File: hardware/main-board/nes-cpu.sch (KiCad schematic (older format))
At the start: 36 parts, among them SW1 NES Reset, U10 74HCT00, U11 PCA9564, U3 74LVC1404, U4 RP2A03, U5 74HCT138, U6 LM4889, U7 AS6C6264, U8 MCP40D17, U9 AT28C64B, Y1 21.5 MHz

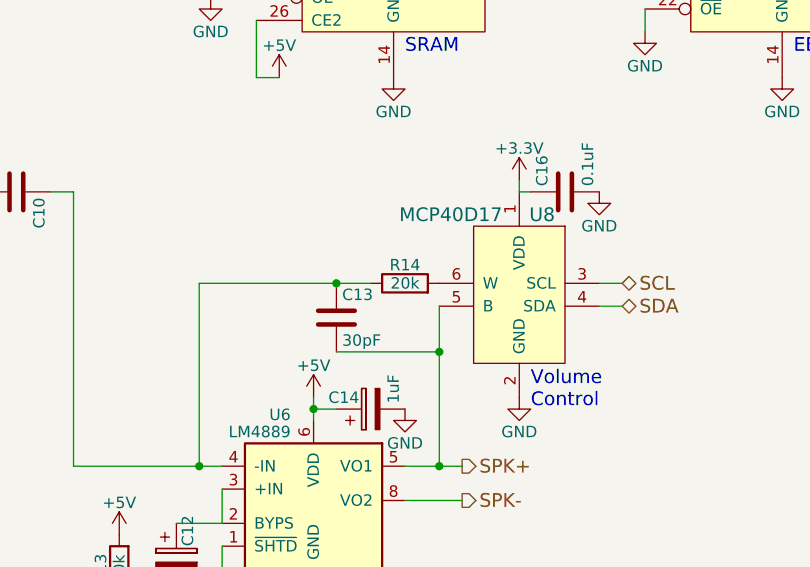
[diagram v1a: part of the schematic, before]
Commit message: Change amplifier gain resistor from 20k to 4.7k
In testing, the minimum volume with 10k was still a little bit too loud,
so going with 4.7k for now. This is easily adjustible in the future
without any actual board layout changes.

Fixes #4
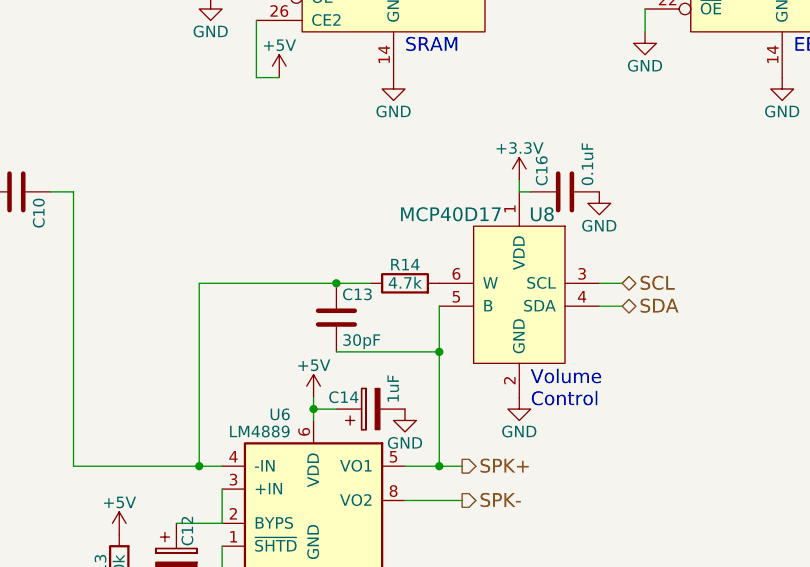
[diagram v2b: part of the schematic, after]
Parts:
- R14: value 20k -> 4.7k; Description RES SMD 20K OHM 5% 1/8W 0805 -> RES SMD 4.7K OHM 5% 1/8W 0805; Manufacturer PN CRCW080520K0JNEA -> CRCW08054K70JNEA; Supplier PN 541-20KACT-ND -> 541-4.7KACT-ND
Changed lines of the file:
@@
 P 6300 3950
 F 0 "R14" V 6380 3950 50  0000 C CNN
-F 1 "20k" V 6300 3950 50  0000 C CNN
+F 1 "4.7k" V 6300 3950 50  0000 C CNN
 F 2 "Resistor_SMD:R_0805_2012Metric" V 6230 3950 50  0001 C CNN
 F 3 "http://www.vishay.com/docs/20035/dcrcwe3.pdf" H 6300 3950 50  0001 C CNN
-F 4 "RES SMD 20K OHM 5% 1/8W 0805" H 6300 3950 60  0001 C CNN "Description"
+F 4 "RES SMD 4.7K OHM 5% 1/8W 0805" H 6300 3950 60  0001 C CNN "Description"
 F 5 "Vishay Dale" H 6300 3950 60  0001 C CNN "Manufacturer"
-F 6 "CRCW080520K0JNEA" H 6300 3950 60  0001 C CNN "Manufacturer PN"
+F 6 "CRCW08054K70JNEA" H 6300 3950 60  0001 C CNN "Manufacturer PN"
 F 7 "Digi-Key" H 6380 4050 50  0001 C CNN "Supplier"
-F 8 "541-20KACT-ND" H 6300 3950 60  0001 C CNN "Supplier PN"
+F 8 "541-4.7KACT-ND" H 6300 3950 60  0001 C CNN "Supplier PN"
 	1    6300 3950
 	0    -1   -1   0

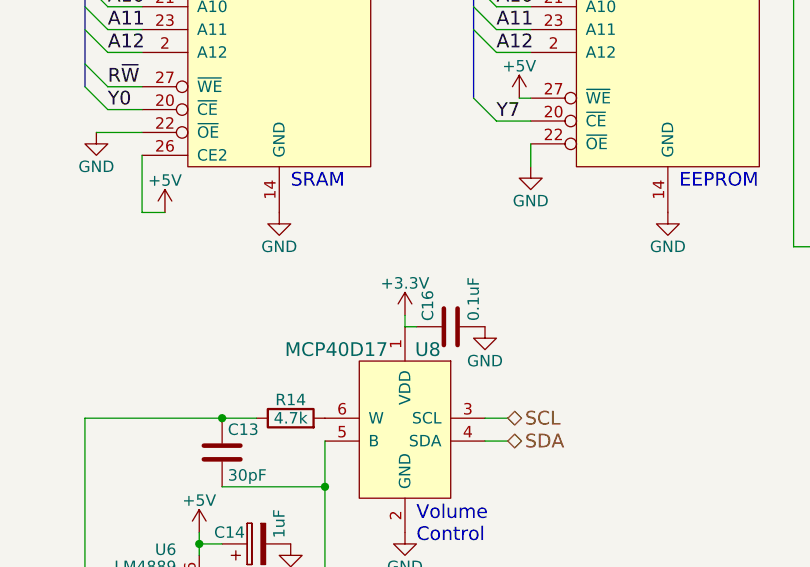
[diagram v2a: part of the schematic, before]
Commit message: Changed U8 Vdd from 3.3V to 5V
Had to reroute a few other traces in the process of doing this, and was
able to remove some vias from a 3.3V line. Also added some stitching
vias to re-connect the ground plane that changed as a result.
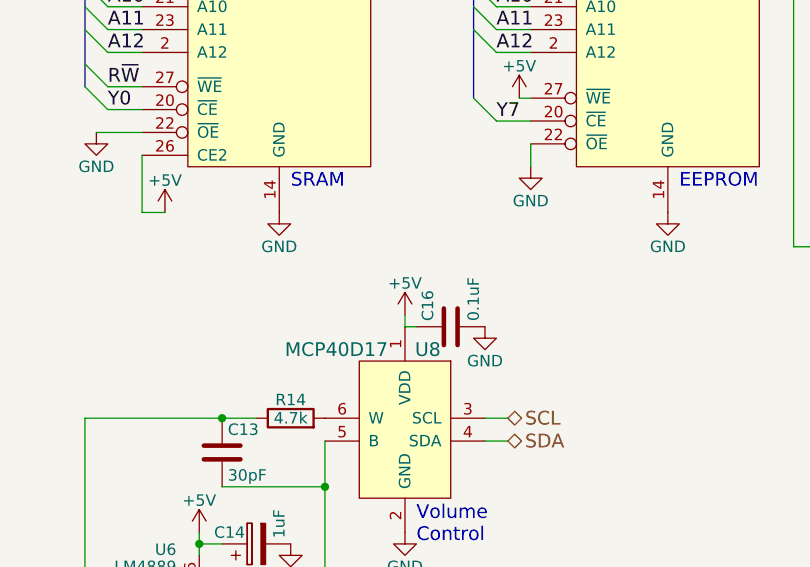
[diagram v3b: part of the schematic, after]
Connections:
- net +3V3: no longer C16.1, U8.1 (VDD)
- net +5V: now also C16.1, U8.1 (VDD)
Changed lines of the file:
@@
-$EndComp
-$Comp
-L +3.3V #PWR051
-U 1 1 5A64F776
-P 6800 3500
-F 0 "#PWR051" H 6800 3350 50  0001 C CNN
-F 1 "+3.3V" H 6800 3640 50  0000 C CNN
-F 2 "" H 6800 3500 50  0001 C CNN
-F 3 "" H 6800 3500 50  0001 C CNN
-	1    6800 3500
-	1    0    0    -1
 $EndComp
 $Comp
@@
 Text Notes 600  1850 0    60   ~ 0
 Reset Button
+$Comp
+L +5V #PWR?
+U 1 1 5B2AA23C
+P 6800 3500
+F 0 "#PWR?" H 6800 3350 50  0001 C CNN
+F 1 "+5V" H 6800 3640 50  0000 C CNN
+F 2 "" H 6800 3500 50  0001 C CNN
+F 3 "" H 6800 3500 50  0001 C CNN
+	1    6800 3500
+	1    0    0    -1
+$EndComp
 $EndSCHEMATC

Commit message: Change U7 footprint to one that more closely matches the component
This involved adding a custom SOIC-28 footprint variant for the
AS6C6264.

This IC uses what it calls a "28-pin 330 mil SOP" package, which is not
in the standard libraries. Its closest match is KiCad's SOIC-28W, but it
is slightly wider and taller. This footprint and 3D model is based on
using the IC's datasheet and the reference datasheets from KiCad's
footprint and 3D model to determine small adjustments.

The replacement footprint is slightly wider, so some routing was
adjusted. However, it is mostly a drop-in replacement.

Fixes #1
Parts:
- U7: footprint Package_SO:SOIC-28W_7.5x17.9mm_P1.27mm -> lib_fp:SOIC-28W_8.636x18.491mm_P1.27mm
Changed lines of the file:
@@
 F 0 "U7" H 6250 2150 60  0000 C CNN
 F 1 "AS6C6264" H 6250 1950 60  0000 C CNN
-F 2 "Package_SO:SOIC-28W_7.5x17.9mm_P1.27mm" H 6250 1950 60  0001 C CNN
+F 2 "lib_fp:SOIC-28W_8.636x18.491mm_P1.27mm" H 6250 1950 60  0001 C CNN
 F 3 "https://www.alliancememory.com/wp-content/uploads/pdf/Alliance%20Memory_64K_AS6C6264v2.0July2017.pdf" H 6250 1950 60  0001 C CNN
 F 4 "IC SRAM 64KBIT 55NS 28SOP" H 6250 1950 60  0001 C CNN "Description"

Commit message: Swap U11 from SOIC to TSSOP footprint
This was a trivial part change, with quite extensive trace routing
changes.

Fixes #2
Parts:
- U11: footprint Package_SO:SOIC-20W_7.5x12.8mm_P1.27mm -> Package_SO:TSSOP-20_4.4x6.5mm_P0.65mm
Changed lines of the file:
@@
 F 0 "U11" H 9600 1850 60  0000 C CNN
 F 1 "PCA9564" H 9600 1750 60  0000 C CNN
-F 2 "Package_SO:SOIC-20W_7.5x12.8mm_P1.27mm" H 9550 1900 60  0001 C CNN
+F 2 "Package_SO:TSSOP-20_4.4x6.5mm_P0.65mm" H 9550 1900 60  0001 C CNN
 F 3 "https://www.nxp.com/docs/en/data-sheet/PCA9564.pdf" H 9550 1900 60  0001 C CNN
 F 4 "IC CTRL PARALLEL/I2C BUS 20-SOIC" H 9600 1650 60  0001 C CNN "Description"
-F 5 "PCA9564D,112" H 9600 1650 60  0001 C CNN "Manufacturer PN"
-F 6 "NXP" H 9600 1650 60  0001 C CNN "Manufacturer"
-F 7 "568-1062-5-ND" H 9600 1650 60  0001 C CNN "Supplier PN"
-F 8 "Digi-Key" H 9600 1650 60  0001 C CNN "Supplier"
+F 5 "NXP" H 9600 1650 60  0001 C CNN "Manufacturer"
+F 6 "PCA9564D,112" H 9600 1650 60  0001 C CNN "Manufacturer PN"
+F 7 "Digi-Key" H 9600 1650 60  0001 C CNN "Supplier"
+F 8 "568-1062-5-ND" H 9600 1650 60  0001 C CNN "Supplier PN"
 	1    9600 1650
 	1    0    0    -1

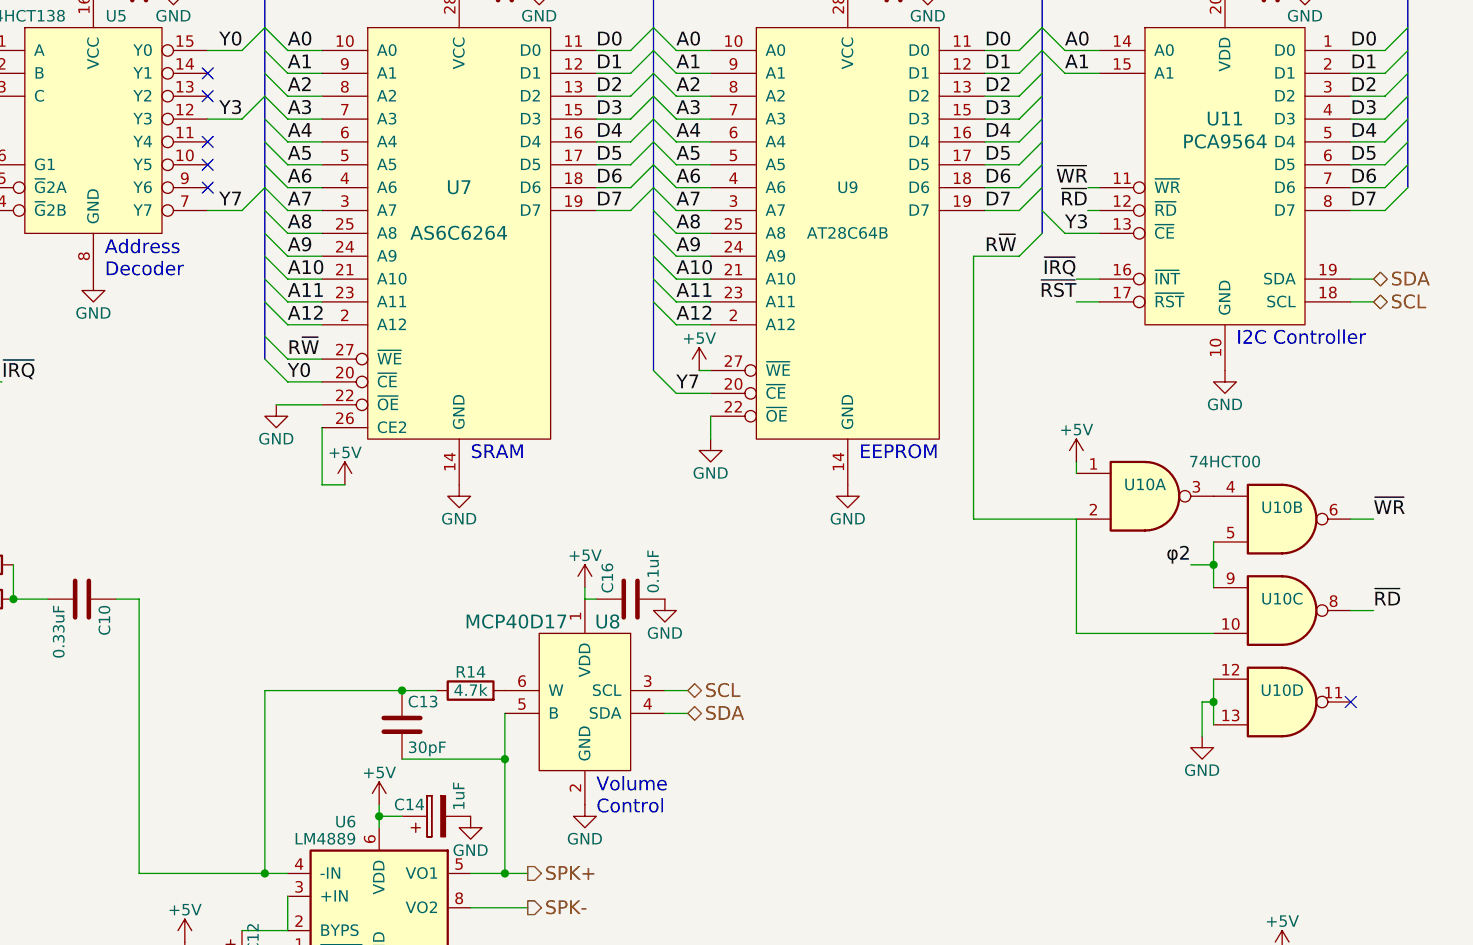
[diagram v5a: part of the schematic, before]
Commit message: Change SRAM address decoding to mirror it onto address $C000
To support the NES APU's DMC feature, we need sample memory placed
around address $C000. Since we're only using a tiny portion of our RAM,
the easiest way is to mirror the RAM onto both $0000 and $C000.

This can be accomplished with a spare NAND gate already in our circuit,
and the secondary non-inverting chip enable line of the SRAM chip. The
idea is that if either Y0 or Y6 is low, then the output of the NAND gate
will be high, and thus select the chip.

Fixes #7
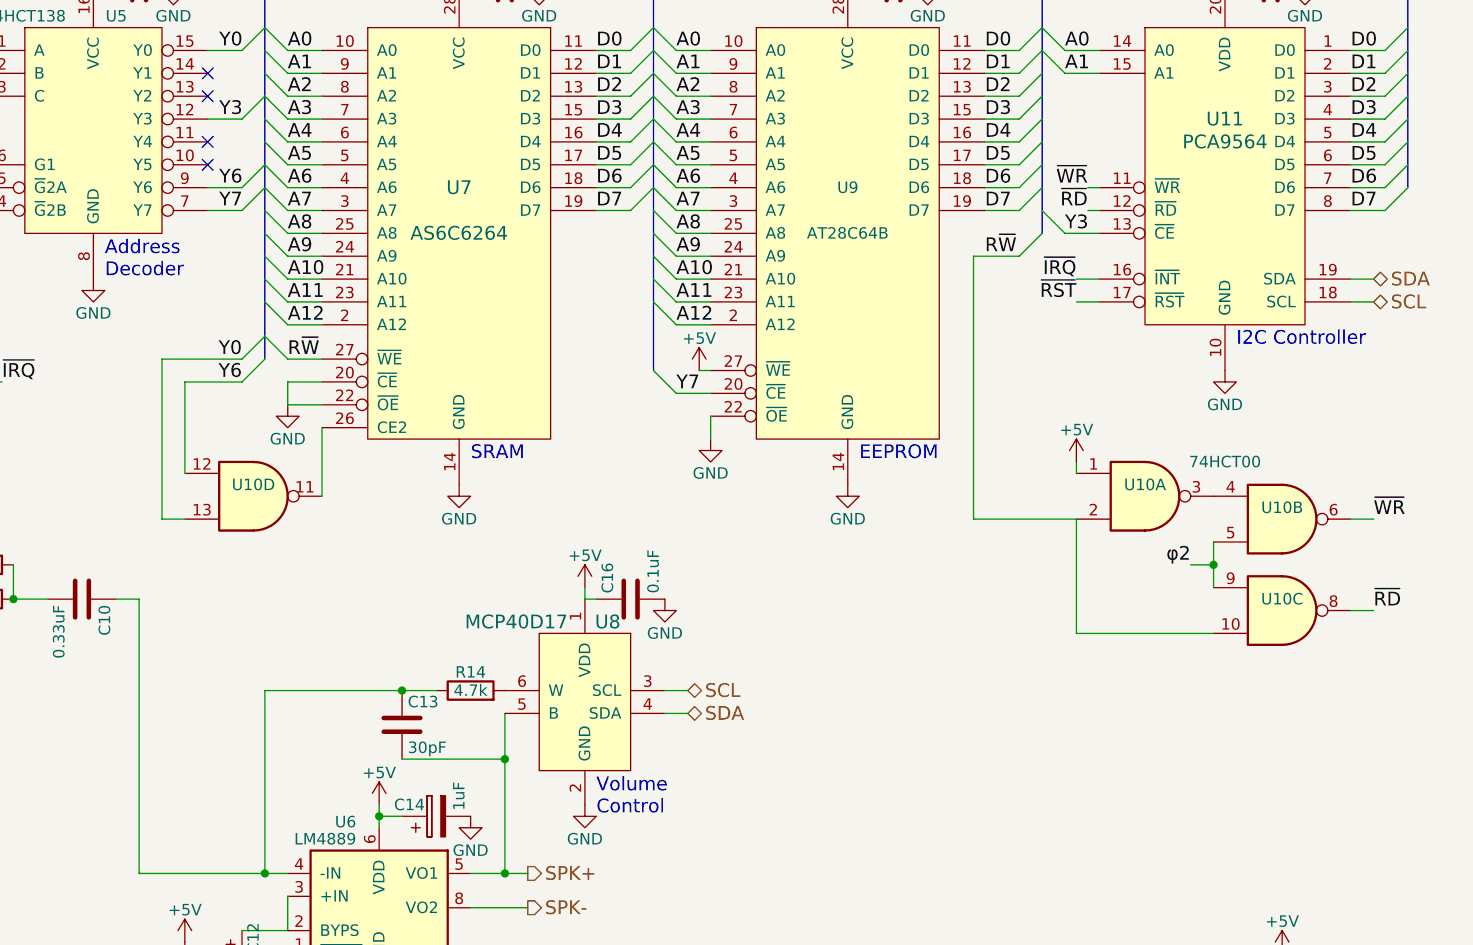
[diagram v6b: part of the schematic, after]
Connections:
- net +5V: no longer U7.26 (CE2)
- net GND: now also U7.20 (~CE); no longer U10.12, U10.13
- net Y0: now also U10.13; no longer U7.20 (~CE)
- net Y6: now reaches U5.9 (Y6)
- net Y6: now also U10.12
- net at U10.11: now also U7.26 (CE2)
- no-connect marks 10 -> 8
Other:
- moved on the sheet: U10D
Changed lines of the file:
@@
-$EndComp
-$Comp
-L +5V #PWR030
-U 1 1 5A482A40
-P 5750 3050
-F 0 "#PWR030" H 5750 2900 50  0001 C CNN
-F 1 "+5V" H 5750 3190 50  0000 C CNN
-F 2 "" H 5750 3050 50  0001 C CNN
-F 3 "" H 5750 3050 50  0001 C CNN
-	1    5750 3050
-	1    0    0    -1
 $EndComp
 $Comp
 L GND #PWR031
 U 1 1 5A482A78
-P 5450 2700
-F 0 "#PWR031" H 5450 2450 50  0001 C CNN
-F 1 "GND" H 5450 2550 50  0000 C CNN
-F 2 "" H 5450 2700 50  0001 C CNN
-F 3 "" H 5450 2700 50  0001 C CNN
-	1    5450 2700
+P 5500 2700
+F 0 "#PWR031" H 5500 2450 50  0001 C CNN
+F 1 "GND" H 5500 2550 50  0000 C CNN
+F 2 "" H 5500 2700 50  0001 C CNN
+F 3 "" H 5500 2700 50  0001 C CNN
+	1    5500 2700
 	1    0    0    -1
 $EndComp
@@
 Text Label 5200 1150 0    60   ~ 0
 Y0
-Text Label 5500 2600 0    60   ~ 0
+Text Label 5300 2500 2    60   ~ 0
 Y0
 Text Label 5200 1450 0    60   ~ 0
@@
 	4650 850  4700 850
 Wire Wire Line
-	5650 2700 5450 2700
-Wire Wire Line
 	7350 2750 7350 2850
-Wire Wire Line
-	5650 2800 5650 3050
-Wire Wire Line
-	5650 3050 5750 3050
 Wire Wire Line
 	3650 2900 3700 2900
@@
 	9550 3300 9550 3500
 Wire Wire Line
-	5500 2600 5650 2600
-Wire Wire Line
 	5300 1150 5150 1150
 Wire Wire Line
@@
 Entry Wire Line
 	10300 1850 10400 1750
-Entry Wire Line
-	5400 2500 5500 2600
 Entry Wire Line
 	5300 1150 5400 1050
@@
 NoConn ~ 5150 1550
 NoConn ~ 5150 1650
-NoConn ~ 5150 1750
 $Comp
 L 74HCT00 U10
 U 4 1 5A5C869E
-P 9850 4000
-F 0 "U10" H 9850 4050 50  0000 C CNN
-F 1 "74HCT00" H 9850 3950 50  0001 C CNN
-F 2 "Package_SO:SOIC-14_3.9x8.7mm_P1.27mm" H 9850 4000 50  0001 C CNN
-F 3 "http://www.ti.com/lit/ds/symlink/sn74hct00.pdf" H 9850 4000 50  0001 C CNN
-F 4 "IC GATE NAND 4CH 2-INP 14-SOIC" H 9850 4150 50  0001 C CNN "Description"
-F 5 "Texas Instruments" H 9850 4150 50  0001 C CNN "Manufacturer"
-F 6 "SN74HCT00DR" H 9850 4150 50  0001 C CNN "Manufacturer PN"
-F 7 "Digi-Key" H 9850 4150 50  0001 C CNN "Supplier"
-F 8 "296-14860-1-ND" H 9850 4150 50  0001 C CNN "Supplier PN"
-	4    9850 4000
-	1    0    0    -1
-$EndComp
-$Comp
-L GND #PWR050
-U 1 1 5A5C8B93
-P 9500 4150
-F 0 "#PWR050" H 9500 3900 50  0001 C CNN
-F 1 "GND" H 9500 4000 50  0000 C CNN
-F 2 "" H 9500 4150 50  0001 C CNN
-F 3 "" H 9500 4150 50  0001 C CNN
-	1    9500 4150
-	1    0    0    -1
-$EndComp
-Wire Wire Line
-	9550 3900 9550 4100
-Wire Wire Line
-	9550 4000 9500 4000
-Wire Wire Line
-	9500 4000 9500 4150
-Connection ~ 9550 4000
-NoConn ~ 10150 4000
+P 5350 3100
+F 0 "U10" H 5350 3150 50  0000 C CNN
+F 1 "74HCT00" H 5350 3050 50  0001 C CNN
+F 2 "Package_SO:SOIC-14_3.9x8.7mm_P1.27mm" H 5350 3100 50  0001 C CNN
+F 3 "http://www.ti.com/lit/ds/symlink/sn74hct00.pdf" H 5350 3100 50  0001 C CNN
+F 4 "IC GATE NAND 4CH 2-INP 14-SOIC" H 5350 3250 50  0001 C CNN "Description"
+F 5 "Texas Instruments" H 5350 3250 50  0001 C CNN "Manufacturer"
+F 6 "SN74HCT00DR" H 5350 3250 50  0001 C CNN "Manufacturer PN"
+F 7 "Digi-Key" H 5350 3250 50  0001 C CNN "Supplier"
+F 8 "296-14860-1-ND" H 5350 3250 50  0001 C CNN "Supplier PN"
+	4    5350 3100
+	1    0    0    -1
+$EndComp
 Text HLabel 10250 2150 2    60   BiDi ~ 0
 SDA
@@
 	1    0    0    -1
 $EndComp
+Entry Wire Line
+	5300 1750 5400 1650
+Wire Wire Line
+	5300 1750 5150 1750
+Text Label 5200 1750 0    60   ~ 0
+Y6
+Wire Wire Line
+	5650 2700 5500 2700
+Wire Wire Line
+	5650 2600 5500 2600
+Wire Wire Line
+	5500 2600 5500 2700
+Wire Wire Line
+	5650 3100 5650 2800
+Entry Wire Line
+	5300 2500 5400 2400
+Entry Wire Line
+	5300 2600 5400 2500
+Text Label 5300 2600 2    60   ~ 0
+Y6
+Wire Wire Line
+	5300 2600 5050 2600
+Wire Wire Line
+	5050 2600 5050 3000
+Wire Wire Line
+	5300 2500 4950 2500
+Wire Wire Line
+	4950 2500 4950 3200
+Wire Wire Line
+	4950 3200 5050 3200
 $EndSCHEMATC
